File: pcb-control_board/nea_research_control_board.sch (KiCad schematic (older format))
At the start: 18 parts, among them P1 Rpi_HDR-40, P2 CONN_02X30, U1 AD7683, U2 ADG706, U3 ADG706, U4 ADG706, U5 ADG706, U6 ADG706, U7 ADG706, U8 TPS73133

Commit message: -changed die_holder_block depth from 41mm to 40mm -added a probe block that is a one-piece design thick enough to hold spring probes
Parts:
- added C? (x2): 0.1uF, footprints_on_Cdrive:0402, symbol CAP_NP
- added C?: 10uF, footprints_on_Cdrive:0402, symbol CAP_NP
- added C? (x7): 0.1uF, Resistors_SMD:R_0603_HandSoldering, symbol CAP_NP
- added D1: LED_SMT, footprints:0603-D, symbol LED_SMT
- added P?: CONN_02X05, symbol CONN_02X05
- added R2: 1.5K, footprints_on_Cdrive:0603, symbol Res1_1
- added R?: 1K, footprints_on_Cdrive:0402, symbol Res1_1
- added U? (x4): 74LS08, symbol 74LS08
- added U?: MCP4921, footprints_on_Cdrive:, symbol MCP4921
- C1, C2: footprint footprints_on_Cdrive:0402 -> Resistors_SMD:R_0603_HandSoldering; description CAP CER 0.1UF 16V X5R 0402 -> CAP CER 0.1UF 16V X7R 0603; manufacturer pn 0402YD104KAT2A -> GRM188R71C104KA01D; supplier pn 478-1126-1-ND -> 490-1532-1-ND
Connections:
- net labels added: 5V_OUT, DAC_OUT, GPIO12, GPIO16, GPIO20, GPIO21, GPIO22, GPIO24, GPIO25, GPIO5, GPIO6, SIMO_SDA, SPI_CLK, V2P5, gnd_mux_en, ~ADC_CS, ~DAC_CS
- net labels removed: ADC_CS, CLK_SW, V1P25, ~CS_SW
- wire segments 285 -> 356
- no-connect marks 24 -> 27
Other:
- note added: "Bypass Caps"
- note added: "spare"
- moved on the sheet: C4, C5, C6, P1, TP1, U8

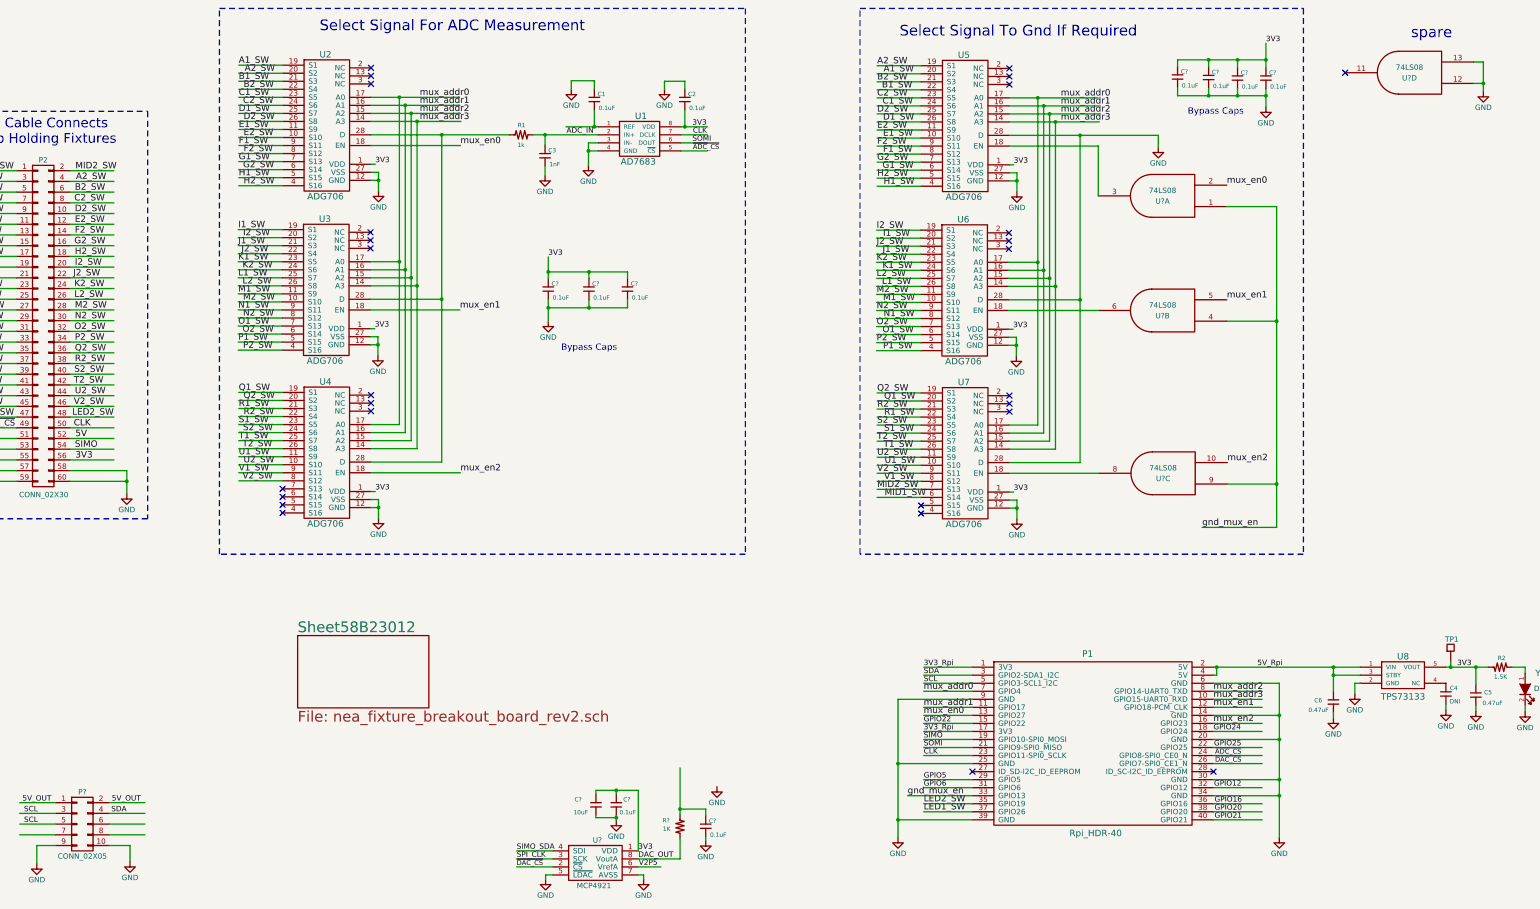
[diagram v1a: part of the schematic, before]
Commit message: -working on new pcb for research test fixture that will sit on top of the breakout board headers. This new pcb will use an msp430 to control measurements at each sensor and will communicate with a raspberry pi via the I2C interface on UCB0 of the msp430. Schematic is rough but almost complete.
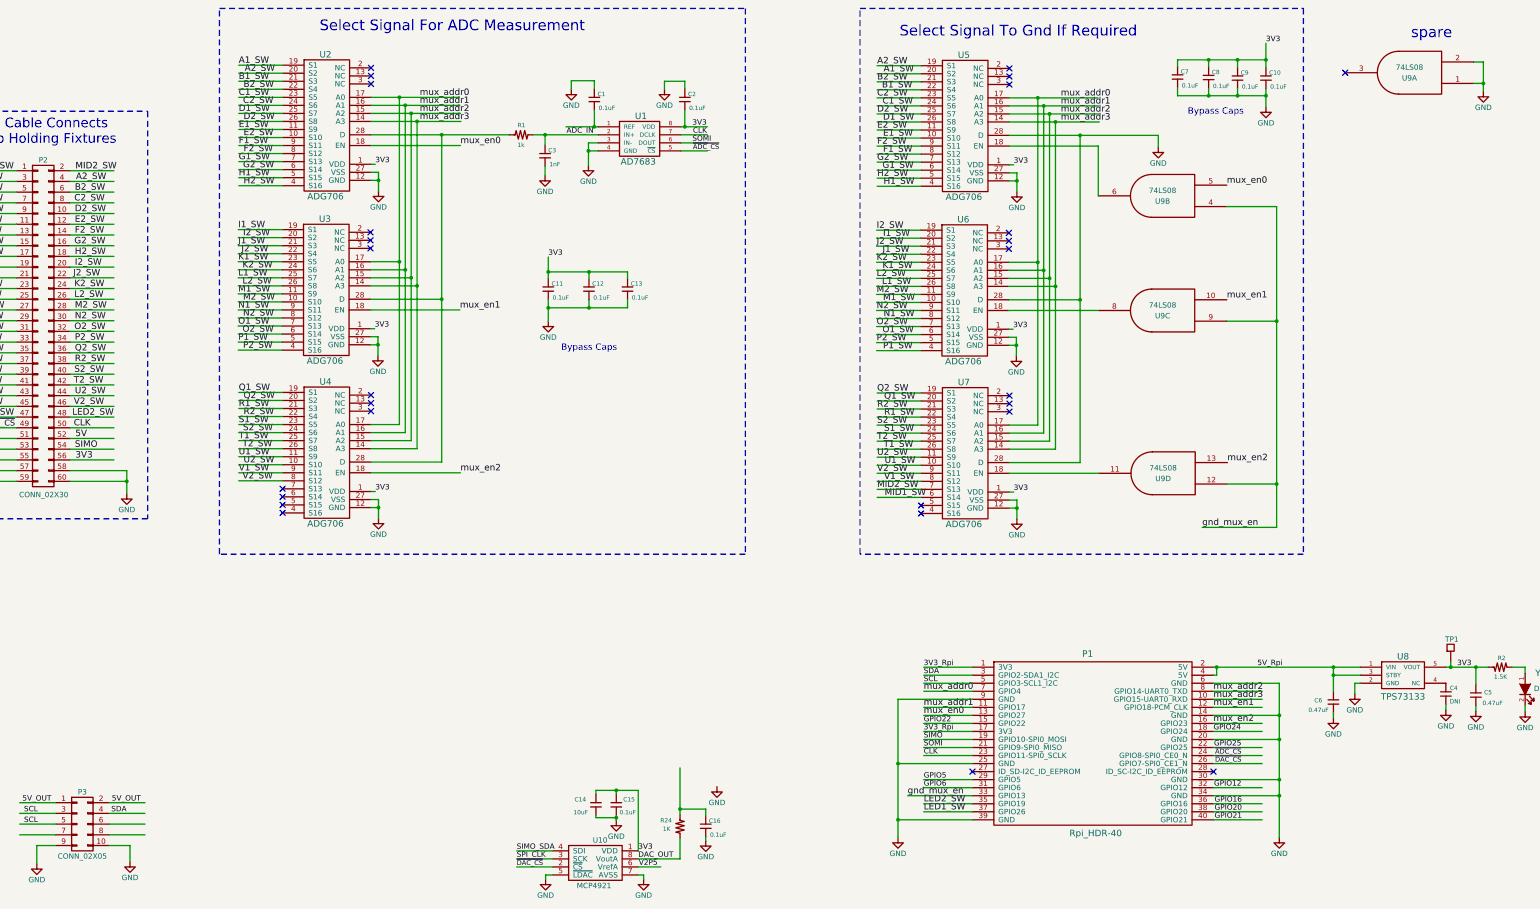
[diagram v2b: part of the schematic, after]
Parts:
- U9: renamed from U?; footprint (none) -> footprints_on_Cdrive:SOIC-14_N; description (none) -> IC GATE AND 4CH 2-INP 14-SO; manufacturer (none) -> Diodes Inc.; manufacturer pn (none) -> 74HC08S14-13; supplier (none) -> digikey; supplier pn (none) -> 74HC08S14-13DICT-ND
- gave numbers to parts that had none: 14
